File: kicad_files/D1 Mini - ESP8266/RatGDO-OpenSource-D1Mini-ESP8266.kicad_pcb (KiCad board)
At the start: 2 copper layers, 55 x 70 mm, 13 parts, among them J1 Screw_Terminal_01x03, J2 Screw_Terminal_01x03, J3 Screw_Terminal_01x03, Q1 2N7002, Q2 AO3400A, U1 WeMos_D1_mini

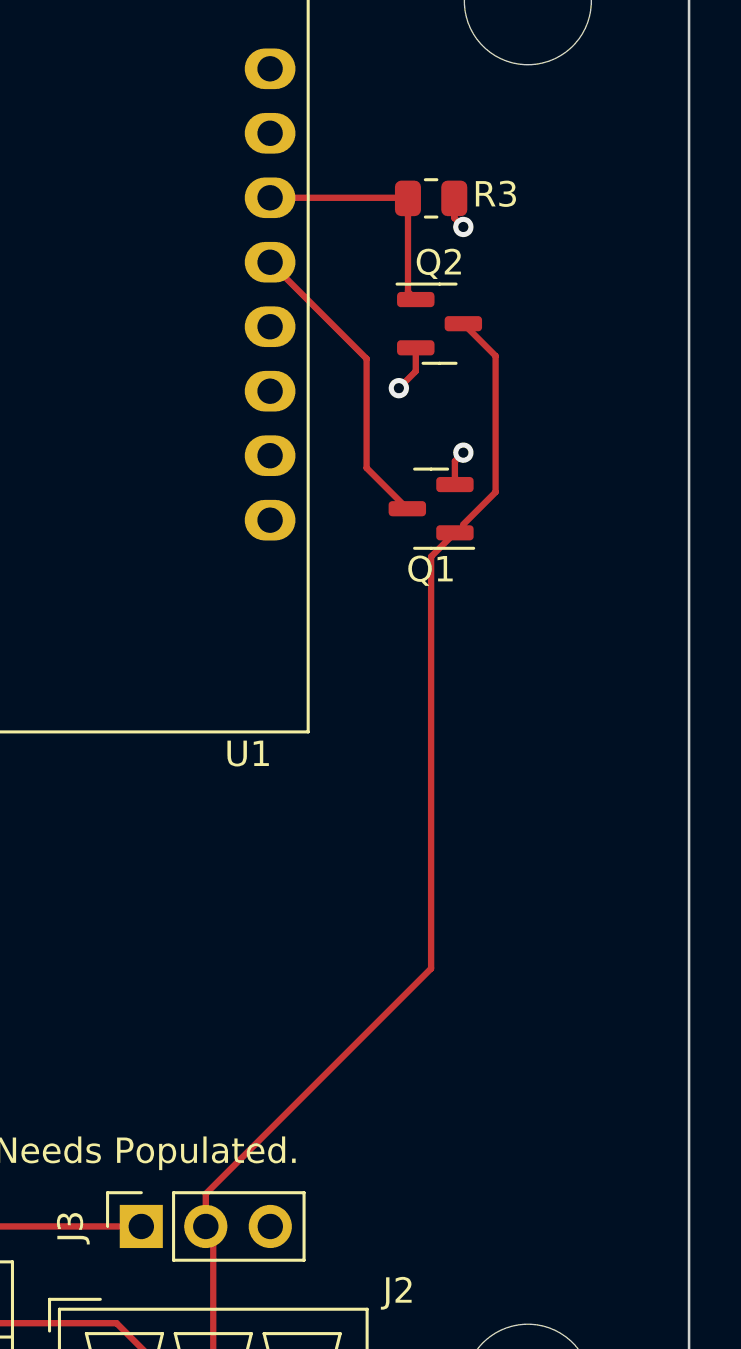
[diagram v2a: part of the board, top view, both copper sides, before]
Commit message: Cleaning up Schematics and making PCB layout similar for D1 Boards
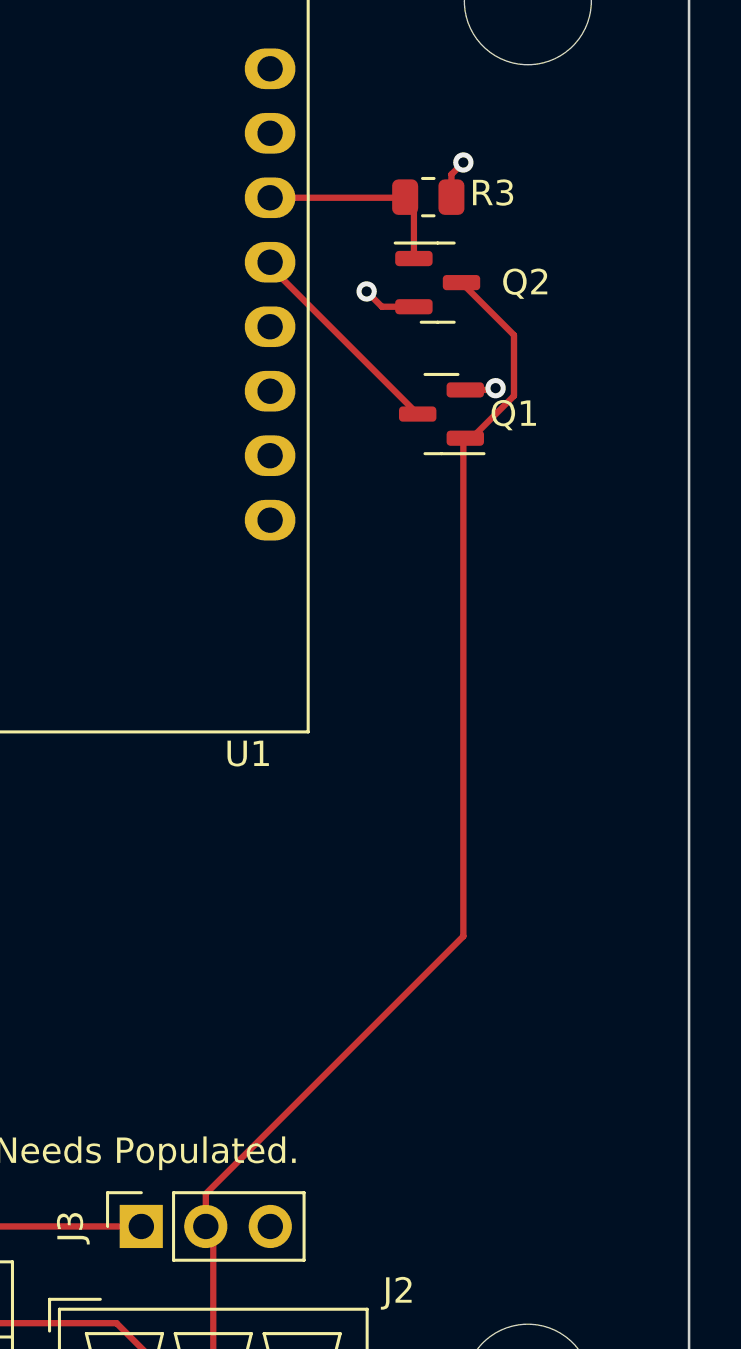
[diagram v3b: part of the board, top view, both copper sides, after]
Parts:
- moved Q1 3.75 mm to (159.2, 79.8)
- moved Q2 1.62 mm to (159.0, 74.6)
- moved R3 0.12 mm to (158.6, 71.2)
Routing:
- net Net-(Q1-D): track 11.9 -> 8.39 mm
- net Net-(J1-Red/Cntrl): track 66.3 -> 69.3 mm
- net Net-(Q2-G): track 9.55 -> 7.89 mm
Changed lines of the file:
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@@
   (net 18 "Net-(J1-Red{slash}Cntrl)")
   (footprint "Resistor_SMD:R_0805_2012Metric" (layer "F.Cu")
-    (at 158.75 71.264162 180)
+    (at 158.638673 71.215222 180)
     (descr "Resistor SMD 0805 (2012 Metric), square (rectangular) end terminal, IPC_7351 nominal, (Body size source: IPC-SM-782 page 72, https://www.pcb-3d.com/wordpress/wp-content/uploads/ipc-sm-782a_amendment_1_and_2.pdf), generated with kicad-footprint-generator")
     (tags "resistor")
@@
   )
   (footprint "Package_TO_SOT_SMD:SOT-23" (layer "F.Cu")
-    (at 159.0825 76.2)
+    (at 159.009257 74.582843)
     (descr "SOT, 3 Pin (https://www.jedec.org/system/files/docs/to-236h.pdf variant AB), generated with kicad-footprint-generator ipc_gullwing_generator.py")
     (tags "SOT TO_SOT_SMD")
@@
     (property "ki_keywords" "N-Channel MOSFET")
     (attr smd)
-    (fp_text reference "Q2" (at 0 -2.4) (layer "F.SilkS")
+    (fp_text reference "Q2" (at 3.4775 0) (layer "F.SilkS")
         (effects (font (size 1 1) (thickness 0.15)))
     )
@@
   )
   (footprint "Package_TO_SOT_SMD:SOT-23" (layer "F.Cu")
-    (at 158.75 83.4875 180)
+    (at 159.1587 79.759515 180)
     (descr "SOT, 3 Pin (https://www.jedec.org/system/files/docs/to-236h.pdf variant AB), generated with kicad-footprint-generator ipc_gullwing_generator.py")
     (tags "SOT TO_SOT_SMD")
@@
     (property "ki_keywords" "N-Channel Switching MOSFET")
     (attr smd)
-    (fp_text reference "Q1" (at 0 -2.4) (layer "F.SilkS")
+    (fp_text reference "Q1" (at -2.8725 0) (layer "F.SilkS")
         (effects (font (size 1 1) (thickness 0.15)))
     )
@@
     (effects (font (size 1 1) (thickness 0.15)) (justify bottom))
   )
-  (segment (start 157.8125 83.4875) (end 156.21 81.885) (width 0.25) (layer "F.Cu") (net 1))
-  (segment (start 156.21 77.5825) (end 152.4075 73.78) (width 0.25) (layer "F.Cu") (net 1))
-  (segment (start 156.21 81.885) (end 156.21 77.5825) (width 0.25) (layer "F.Cu") (net 1))
-  (segment (start 157.813338 71.24) (end 152.4075 71.24) (width 0.25) (layer "F.Cu") (net 2))
-  (segment (start 157.8375 71.264162) (end 157.813338 71.24) (width 0.25) (layer "F.Cu") (net 2))
-  (segment (start 158.145 75.25) (end 157.8375 74.9425) (width 0.25) (layer "F.Cu") (net 2))
-  (segment (start 157.8375 74.9425) (end 157.8375 71.264162) (width 0.25) (layer "F.Cu") (net 2))
+  (segment (start 158.2212 79.759515) (end 152.4075 73.945815) (width 0.25) (layer "F.Cu") (net 1))
+  (segment (start 152.4075 73.945815) (end 152.4075 73.78) (width 0.25) (layer "F.Cu") (net 1))
+  (segment (start 157.701395 71.24) (end 157.726173 71.215222) (width 0.25) (layer "F.Cu") (net 2))
+  (segment (start 158.071757 71.560806) (end 158.071757 73.632843) (width 0.25) (layer "F.Cu") (net 2))
+  (segment (start 152.4075 71.24) (end 157.701395 71.24) (width 0.25) (layer "F.Cu") (net 2))
+  (segment (start 157.726173 71.215222) (end 158.071757 71.560806) (width 0.25) (layer "F.Cu") (net 2))
   (segment (start 124.2225 78.86) (end 129.5475 78.86) (width 0.25) (layer "F.Cu") (net 3))
   (segment (start 124.1025 78.74) (end 124.2225 78.86) (width 0.25) (layer "F.Cu") (net 3))
   (segment (start 124.1025 82.55) (end 124.1025 78.74) (width 0.25) (layer "F.Cu") (net 3))
   (segment (start 129.66 81.4) (end 129.5475 81.4) (width 0.25) (layer "F.Cu") (net 9))
-  (segment (start 159.6875 82.5375) (end 159.6875 81.6125) (width 0.25) (layer "F.Cu") (net 15))
-  (segment (start 159.6875 81.6125) (end 160.02 81.28) (width 0.25) (layer "F.Cu") (net 15))
-  (segment (start 159.6625 71.264162) (end 159.6625 72.0325) (width 0.25) (layer "F.Cu") (net 15))
-  (segment (start 158.145 78.075) (end 157.48 78.74) (width 0.25) (layer "F.Cu") (net 15))
-  (segment (start 158.145 77.15) (end 158.145 78.075) (width 0.25) (layer "F.Cu") (net 15))
+  (segment (start 156.812843 75.532843) (end 156.21 74.93) (width 0.25) (layer "F.Cu") (net 15))
   (segment (start 122.2775 78.74) (end 122.2775 79.6525) (width 0.25) (layer "F.Cu") (net 15))
-  (segment (start 159.6625 72.0325) (end 160.02 72.39) (width 0.25) (layer "F.Cu") (net 15))
+  (segment (start 160.0962 78.809515) (end 161.220485 78.809515) (width 0.25) (layer "F.Cu") (net 15))
+  (segment (start 158.071757 75.532843) (end 156.812843 75.532843) (width 0.25) (layer "F.Cu") (net 15))
+  (segment (start 161.220485 78.809515) (end 161.29 78.74) (width 0.25) (layer "F.Cu") (net 15))
+  (segment (start 159.551173 71.215222) (end 159.551173 70.318827) (width 0.25) (layer "F.Cu") (net 15))
+  (segment (start 159.551173 70.318827) (end 160.02 69.85) (width 0.25) (layer "F.Cu") (net 15))
   (segment (start 122.2775 79.6525) (end 121.92 80.01) (width 0.25) (layer "F.Cu") (net 15))
-  (via (at 160.02 81.28) (size 0.8) (drill 0.4) (layers "F.Cu" "B.Cu") (net 15))
-  (via (at 160.02 72.39) (size 0.8) (drill 0.4) (layers "F.Cu" "B.Cu") (net 15))
-  (via (at 157.48 78.74) (size 0.8) (drill 0.4) (layers "F.Cu" "B.Cu") (net 15))
+  (via (at 160.02 69.85) (size 0.8) (drill 0.4) (layers "F.Cu" "B.Cu") (net 15))
+  (via (at 156.21 74.93) (size 0.8) (drill 0.4) (layers "F.Cu" "B.Cu") (net 15))
   (via (at 121.92 80.01) (size 0.8) (drill 0.4) (layers "F.Cu" "B.Cu") (net 15))
+  (via (at 161.29 78.74) (size 0.8) (drill 0.4) (layers "F.Cu" "B.Cu") (net 15))
   (segment (start 136.355 111.76) (end 147.335 111.76) (width 0.25) (layer "F.Cu") (net 17))
   (segment (start 129.7 118.27) (end 129.7 118.415) (width 0.25) (layer "F.Cu") (net 17))
@@
   (segment (start 122.2775 110.8475) (end 129.7 118.27) (width 0.25) (layer "F.Cu") (net 17))
   (segment (start 145.4 120.65) (end 146.67 119.38) (width 0.25) (layer "F.Cu") (net 17))
-  (segment (start 160.02 76.2) (end 161.29 77.47) (width 0.25) (layer "F.Cu") (net 18))
-  (segment (start 149.875 110.475) (end 158.75 101.6) (width 0.25) (layer "F.Cu") (net 18))
+  (segment (start 160.26959 80.785715) (end 162.015 79.040305) (width 0.25) (layer "F.Cu") (net 18))
+  (segment (start 162.015 79.040305) (end 162.015 76.651086) (width 0.25) (layer "F.Cu") (net 18))
   (segment (start 146.36 115.57) (end 150.17 119.38) (width 0.25) (layer "F.Cu") (net 18))
   (segment (start 150.17 119.38) (end 150.17 112.055) (width 0.25) (layer "F.Cu") (net 18))
-  (segment (start 158.75 85.375) (end 159.6875 84.4375) (width 0.25) (layer "F.Cu") (net 18))
+  (segment (start 160.02 80.785715) (end 160.0962 80.709515) (width 0.25) (layer "F.Cu") (net 18))
+  (segment (start 162.015 76.651086) (end 159.946757 74.582843) (width 0.25) (layer "F.Cu") (net 18))
+  (segment (start 160.02 80.785715) (end 160.26959 80.785715) (width 0.25) (layer "F.Cu") (net 18))
   (segment (start 150.17 112.055) (end 149.875 111.76) (width 0.25) (layer "F.Cu") (net 18))
-  (segment (start 161.29 82.835) (end 160.005698 84.119302) (width 0.25) (layer "F.Cu") (net 18))
-  (segment (start 158.75 101.6) (end 158.75 85.375) (width 0.25) (layer "F.Cu") (net 18))
   (segment (start 134.7 118.415) (end 137.545 115.57) (width 0.25) (layer "F.Cu") (net 18))
-  (segment (start 161.29 77.47) (end 161.29 82.835) (width 0.25) (layer "F.Cu") (net 18))
+  (segment (start 149.875 111.76) (end 149.875 110.475) (width 0.25) (layer "F.Cu") (net 18))
   (segment (start 137.545 115.57) (end 146.36 115.57) (width 0.25) (layer "F.Cu") (net 18))
-  (segment (start 149.875 111.76) (end 149.875 110.475) (width 0.25) (layer "F.Cu") (net 18))
+  (segment (start 149.875 110.475) (end 160.02 100.33) (width 0.25) (layer "F.Cu") (net 18))
+  (segment (start 160.02 100.33) (end 160.02 80.785715) (width 0.25) (layer "F.Cu") (net 18))
   (zone (net 15) (net_name "GND") (layer "B.Cu") (hatch edge 0.5)
     (connect_pads (clearance 0.5))

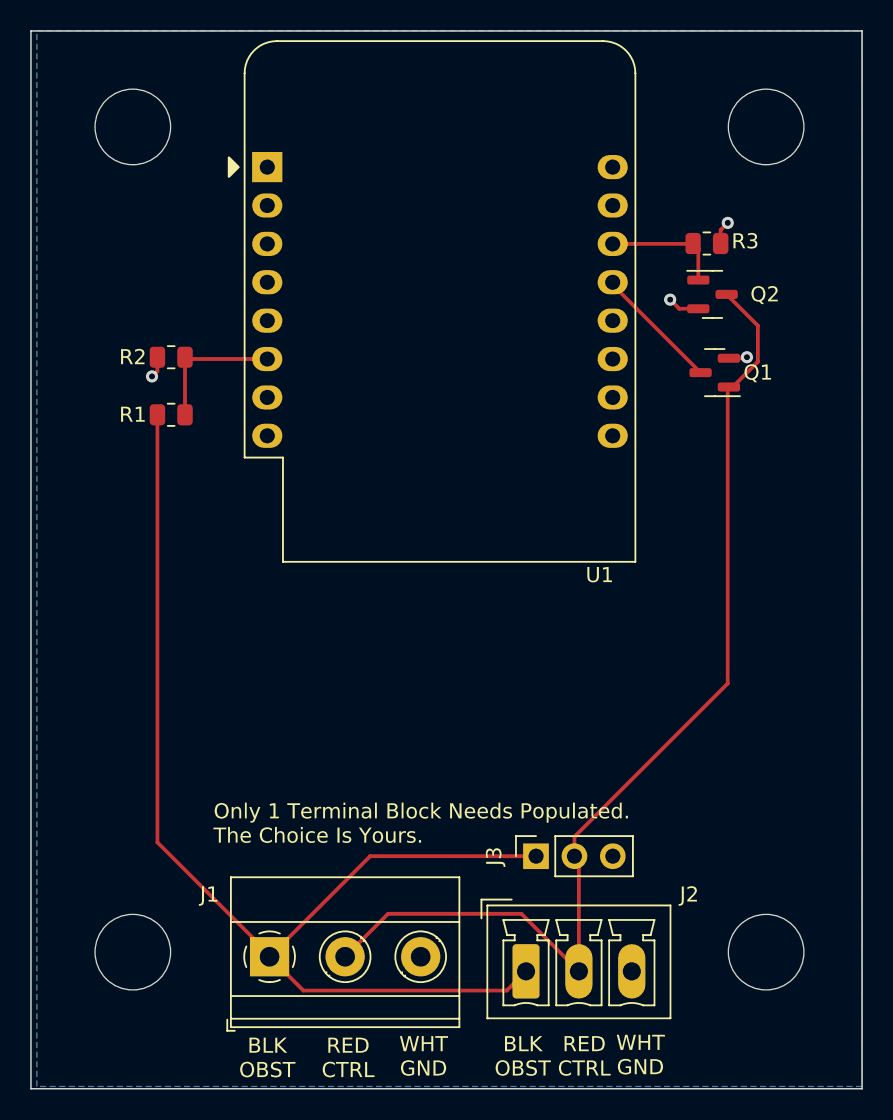
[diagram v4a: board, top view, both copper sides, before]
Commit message: Update ESP8266 schematics and PCB
Added 1K R4 on gate of Q2.
Added 10K R5/R6 on gate of Q1.
Re-laid out PCB, all single sided and smaller.
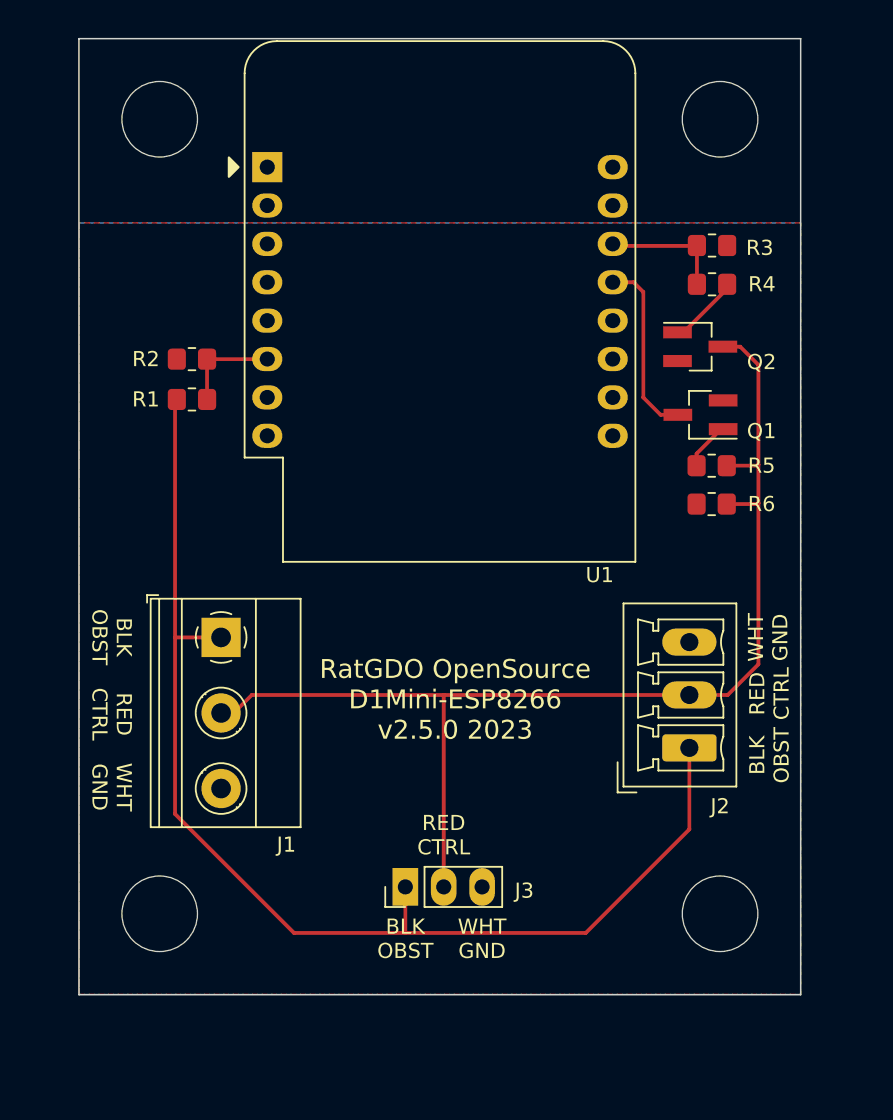
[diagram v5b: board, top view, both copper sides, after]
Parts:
- added R4: 1k, Resistor_SMD:R_0805_2012Metric_Pad1.20x1.40mm_HandSolder, F.Cu at (159.0, 73.9)
- added R5: 10k, Resistor_SMD:R_0805_2012Metric_Pad1.20x1.40mm_HandSolder, F.Cu at (159.0, 85.9)
- added R6: 10k, Resistor_SMD:R_0805_2012Metric_Pad1.20x1.40mm_HandSolder, F.Cu at (159.0, 88.5)
- J3: footprint Connector_PinSocket_2.54mm:PinSocket_1x03_P2.54mm_Vertical -> Connector_PinHeader_2.54mm:PinHeader_1x03_P2.54mm_Vertical
- Q1, Q2: footprint Package_TO_SOT_SMD:SOT-23 -> Package_TO_SOT_SMD:SOT-23_Handsoldering
- R1, R2, R3: footprint Resistor_SMD:R_0805_2012Metric -> Resistor_SMD:R_0805_2012Metric_Pad1.20x1.40mm_HandSolder
- moved J1 21.4 mm to (126.5, 97.3), turned to -90 degrees
- moved J2 18.3 mm to (157.5, 104.6), turned to 90 degrees
- moved J3 8.89 mm to (138.7, 113.8)
- moved REF** 3.97 mm to (159.5, 115.6)
- moved Q2 3.56 mm to (158.2, 78.0)
- moved REF** 3.10 mm to (122.4, 115.6)
- moved REF** 3.09 mm to (159.5, 63.0)
- moved Q1 2.94 mm to (158.2, 82.5)
- moved REF** 1.85 mm to (122.4, 63.0)
- moved R1 1.71 mm to (124.6, 81.5)
- moved R2 1.38 mm to (124.6, 78.9)
- moved R3 0.37 mm to (159.0, 71.3), turned to 0 degrees
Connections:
- net Net-(J1-Blk/Obst) renamed BLK/OBST
- net Net-(Q1-D) renamed /ESP_RX
- J1 pad 2: Net-(J1-Red/Cntrl) -> RED/CTRL
- J2 pad 2: Net-(J1-Red/Cntrl) -> RED/CTRL
- J3 pad 2: Net-(J1-Red/Cntrl) -> RED/CTRL
- Q1 pad 1: Net-(J1-Red/Cntrl) -> Net-(Q1-G)
- Q2 pad 3: Net-(J1-Red/Cntrl) -> RED/CTRL
- R3 pad 1: GND -> /ESP_TX
- R3 pad 2: Net-(Q2-G) -> GND
- U1 pad 14: Net-(Q2-G) -> /ESP_TX
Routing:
- net RED/CTRL: track 0.00 -> 75.7 mm
- net Net-(J1-Red/Cntrl): track 69.3 -> 0.00 mm
- net /ESP_TX: track 0.00 -> 7.86 mm
- net GND: track 6.31 -> 0.00 mm, vias 4 -> 0
- net Net-(Q2-G): track 7.89 -> 4.08 mm
- net /ESP_RX: track 8.39 -> 12.0 mm
- net Net-(Q1-G): track 0.00 -> 3.09 mm
- net Net-(U1-MOSI/D7): track 9.30 -> 6.39 mm
- net BLK/OBST: track 77.8 -> 78.7 mm
- added copper zone on F.Cu, net GND
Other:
- board size 55 x 70 mm -> 47.8 x 63.3 mm
- board text added: "3V3"
- board text added: "5V"
- board text added: "A0"
- board text added: "D0"
- board text added: "D1/SCL"
- board text added: "D2/SDA"
- board text added: "D3"
- board text added: "D4"
- board text added: "D5/SCK"
- board text added: "D6/MISO"
- board text added: "D7/MOSI"
- board text added: "D8"
- board text added: "Only 1 Terminal Block Needs Populating. The Choice Is Yours."
- board text added: "RX"
- board text added: "RatGDO OpenSource D1Mini-ESP8266 v2.5.0 2023"
- board text added: "TX"
- board text removed: "5v"
- board text removed: "EN"
- board text removed: "GPIO0"
- board text removed: "GPIO1"
- board text removed: "GPIO12"
- board text removed: "GPIO13"
- board text removed: "GPIO14"
- board text removed: "GPIO15"
- board text removed: "GPIO16"
- board text removed: "GPIO2"
- board text removed: "GPIO3"
- board text removed: "GPIO4"
- board text removed: "GPIO5"
- board text removed: "Only 1 Terminal Block Needs Populated. The Choice Is Yours."
- board text removed: "VCC-3v3"

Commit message: Update schematics for mini wide board v2.5
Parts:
- renumbered REF** to H1
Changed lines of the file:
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@@
     (descr "Mounting Hole 5mm, no annular")
     (tags "mounting hole 5mm no annular")
-    (attr exclude_from_pos_files exclude_from_bom)
-    (fp_text reference "REF**" (at 0 -6) (layer "F.SilkS") hide
+    (attr board_only exclude_from_pos_files exclude_from_bom)
+    (fp_text reference "H1" (at 0 -6) (layer "F.SilkS") hide
         (effects (font (size 1 1) (thickness 0.15)))
     )
@@
     (descr "Mounting Hole 5mm, no annular")
     (tags "mounting hole 5mm no annular")
-    (attr exclude_from_pos_files exclude_from_bom)
-    (fp_text reference "REF**" (at 0 -6) (layer "F.SilkS") hide
+    (attr board_only exclude_from_pos_files exclude_from_bom)
+    (fp_text reference "H1" (at 0 -6) (layer "F.SilkS") hide
         (effects (font (size 1 1) (thickness 0.15)))
     )
@@
     (descr "Mounting Hole 5mm, no annular")
     (tags "mounting hole 5mm no annular")
-    (attr exclude_from_pos_files exclude_from_bom)
-    (fp_text reference "REF**" (at 0 -6) (layer "F.SilkS") hide
+    (attr board_only exclude_from_pos_files exclude_from_bom)
+    (fp_text reference "H1" (at 0 -6) (layer "F.SilkS") hide
         (effects (font (size 1 1) (thickness 0.15)))
     )
@@
     (descr "Mounting Hole 5mm, no annular")
     (tags "mounting hole 5mm no annular")
-    (attr exclude_from_pos_files exclude_from_bom)
-    (fp_text reference "REF**" (at 0 -6) (layer "F.SilkS") hide
-        (effects (font (size 1 1) (thickness 0.15)))
-    )
+    (attr board_only exclude_from_pos_files exclude_from_bom)
+    (fp_text reference "H1" (at 0 -6) (layer "F.SilkS") hide
+        (effects (font (size 1 1) (thickness 0.15)))
+    )
